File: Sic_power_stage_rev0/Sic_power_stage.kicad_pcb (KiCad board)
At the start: 4 copper layers, 265.1 x 88 mm, 176 parts, among them J1 20021321-00006C4LF, J2 20021321-00006C4LF, J3 20021321-00006C4LF, J4 20021321-00006C4LF, J5 20021321-00006C4LF, J6 20021321-00006C4LF, J7 20021321-00006C4LF, J8 20021321-00006C4LF, Q1 NTBG014N120M3P, Q10 NTBG014N120M3P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

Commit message: Define custom rules
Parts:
- moved STANDOFF19 161.1 mm to (36.5, 34.5)
- moved J1 143.1 mm to (52.5, -14.5)
- moved R12 137.7 mm to (-68.8, 16.9), turned to 180 degrees
- moved STANDOFF11 127.8 mm to (-113.5, -25.8)
- moved STANDOFF13 127.0 mm to (-69.0, 33.0)
- moved STANDOFF14 127.0 mm to (-58.0, 33.0)
- moved HOLE1 125.6 mm to (-270.1, -32.1)
- moved STANDOFF12 91.0 mm to (-80.0, 33.0)
- moved STANDOFF8 83.3 mm to (-113.0, -43.5)
- moved J3 69.0 mm to (-85.5, 23.5)
- moved J4 69.0 mm to (-52.5, 23.5)
- moved R13 40.6 mm to (-76.5, 16.9)
- moved J2 33.7 mm to (-21.5, 10.4)
- moved STANDOFF18 32.3 mm to (-145.0, -47.8)
- moved R6 27.6 mm to (-100.8, 10.2)
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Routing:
- net /Half Bridge A/G_TOP: track 30.7 -> 8.71 mm
- net /Half Bridge B/G_TOP: track 20.6 -> 4.58 mm, vias 0 -> 1
- net /Half Bridge A/S_BOT: track 0.00 -> 15.4 mm, vias 1 -> 0
- net /Half Bridge B/node_a: track 0.00 -> 12.1 mm
- net /Half Bridge B/D_BOT: track 23.8 -> 11.7 mm
- net /Half Bridge B/S_TOP: track 15.7 -> 6.30 mm, vias 0 -> 1
- net /Half Bridge A/D_TOP: track 22.5 -> 15.6 mm, vias 3 -> 2
- net /VBUS_M: track 6.50 -> 0.00 mm
- net /Half Bridge A/G_BOT: track 14.5 -> 20.6 mm, vias 1 -> 0
- net /Half Bridge B/S_BOT: track 6.05 -> 0.00 mm, vias 1 -> 0
- net /Half Bridge A/S_TOP: track 8.07 -> 2.95 mm
- net /Half Bridge B/G_BOT: track 4.58 -> 0.00 mm, vias 1 -> 0
- net PWRGND: track 17.6 -> 14.5 mm
- net /Half Bridge A/NTC_BOT: track 4.48 -> 2.48 mm
- net VBUS: vias 1464 -> 1466

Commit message: Redefine SiC layout
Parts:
- removed Q14, Q15, Q16: NTBG014N120M3P, Package_TO_SOT_SMD:TO-263-7_TabPin8
- removed Q19: IPN70R1K5CEATMA1, smd-semi:SOT-223-3
- removed R52, R53, R54, R55, R56, R57, R58, R59, R60, R61, R62, R63, R64, R65, R66, R67, R68, R69: R-1206, IPC7351-Nominal:RESC3216X60
- removed R70: R-0603, IPC7351-Nominal:RESC1608X50
- moved R20 244.3 mm to (-1.75, 62.2)
- moved R17 230.0 mm to (-4.25, 62.2), turned to -90 degrees
- moved R19 221.5 mm to (0.65, 62.2)
- moved STANDOFF18 218.5 mm to (58.0, 33.0)
- moved R16 208.9 mm to (-6.75, 62.2), turned to -90 degrees
- moved STANDOFF15 197.7 mm to (-106.0, 100.0)
- moved STANDOFF20 193.0 mm to (80.0, 33.0)
- moved HOLE5 178.9 mm to (-141.2, -19.5)
- moved C33 178.7 mm to (99.5, -19.5), turned to 180 degrees
- moved C27 174.4 mm to (-176.2, 37.8)
- moved C28 174.4 mm to (-126.4, 32.9)
- moved C40 174.4 mm to (-159.6, 47.7)
- moved R46 174.4 mm to (-142.4, 24.4)
- moved R47 174.4 mm to (-142.4, 27.7)
- moved R48 174.4 mm to (-142.4, 31.1)
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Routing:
- net /Half Bridge C/S_TOP: track 156.8 -> 0.00 mm, vias 3 -> 0
- net /Half Bridge C/S_BOT: track 129.5 -> 0.00 mm, vias 3 -> 0
- net /Half Bridge C/G_BOT: track 122.0 -> 0.00 mm, vias 2 -> 0
- net /Half Bridge C/G_TOP: track 110.7 -> 0.00 mm, vias 3 -> 0
- net /Half Bridge C/SHUNT-: track 23.5 -> 0.00 mm
- net /Half Bridge B/SHUNT-: track 22.9 -> 0.00 mm
- net /Half Bridge C/SHUNT+: track 22.8 -> 0.00 mm
- net /Half Bridge B/SHUNT+: track 22.2 -> 0.00 mm
- net /Half Bridge A/G_BOT: track 20.6 -> 0.00 mm
- net /Half Bridge A/D_TOP: track 15.6 -> 0.00 mm, vias 2 -> 0
- net /Half Bridge A/S_BOT: track 15.4 -> 0.00 mm
- net /Half Bridge B/D_TOP: track 15.1 -> 0.35 mm, vias 0 -> 1
- net (no net): track 16.7 -> 2.66 mm
- net /Half Bridge B/node_a: track 12.1 -> 0.00 mm
- net /Half Bridge B/D_BOT: track 11.7 -> 0.00 mm
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- added copper zone on F.Cu, net /Half Bridge B/node_a
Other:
- board size 265.1 x 88 mm -> 241.3 x 91 mm

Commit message: Add minor changes
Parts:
- moved D4 88.8 mm to (-62.2, 19.5)
- moved R18 72.9 mm to (20.5, 3.00)
- moved R20 72.3 mm to (19.8, -6.75), turned to 180 degrees
- moved D10 71.6 mm to (42.8, 25.2)
- moved R19 70.5 mm to (-14.0, -6.75), turned to 180 degrees
- moved D7 69.8 mm to (-23.8, 30.5), turned to -90 degrees
- moved R17 59.9 mm to (-12.8, 3.00), turned to 0 degrees
- moved D3 58.8 mm to (-105.8, 9.50), turned to -90 degrees
- moved R6 45.5 mm to (-59.8, 17.5)
- moved D2 35.1 mm to (-57.8, 20.8)
- moved C2 34.7 mm to (-55.2, 18.8)
- moved C10 27.5 mm to (-79.5, -22.0), turned to 90 degrees
- moved C11 27.5 mm to (-60.5, -49.5), turned to -90 degrees
- moved C12 27.5 mm to (-41.5, -22.0), turned to 90 degrees
- moved C22 27.5 mm to (-24.2, -49.5), turned to -90 degrees
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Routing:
- net (no net): track 2.66 -> 0.16 mm
- net PWRGND: track 10.4 -> 8.87 mm
- net Net-(DS1-A): track 1.73 -> 1.00 mm
- net VBUS: track 0.00 -> 0.01 mm, vias 4 -> 1
- removed copper zone on B.Cu, net PWRGND
- removed copper zone on B.Cu, net VBUS

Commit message: Re allocate film capacitors and re define layout for power mosfet
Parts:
- moved C38 10.2 mm to (99.0, -25.0)
- moved C12 9.77 mm to (-50.8, -25.0)
- moved C25 9.01 mm to (24.2, -25.0)
- moved C9 8.50 mm to (-90.5, -52.5)
- moved C22 8.31 mm to (-16.5, -52.5)
- moved C35 6.35 mm to (57.2, -52.8)
- moved C33 4.76 mm to (94.8, -19.2)
- moved C34 4.76 mm to (94.8, -13.2)
- moved C37 4.28 mm to (86.8, -52.5)
- moved C11 3.50 mm to (-62.2, -52.5)
- moved C24 3.35 mm to (12.2, -52.5)
- moved C36 3.35 mm to (70.0, -25.2)
- moved C20 3.20 mm to (20.2, -19.2)
- moved C21 3.20 mm to (20.2, -13.2)
- moved C23 3.09 mm to (-4.50, -25.0)
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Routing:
- added copper zone on B.Cu, net PWRGND
- added copper zone on In1.Cu, net PWRGND
- added copper zone on B.Cu, net VBUS
- added copper zone on In1.Cu, net VBUS

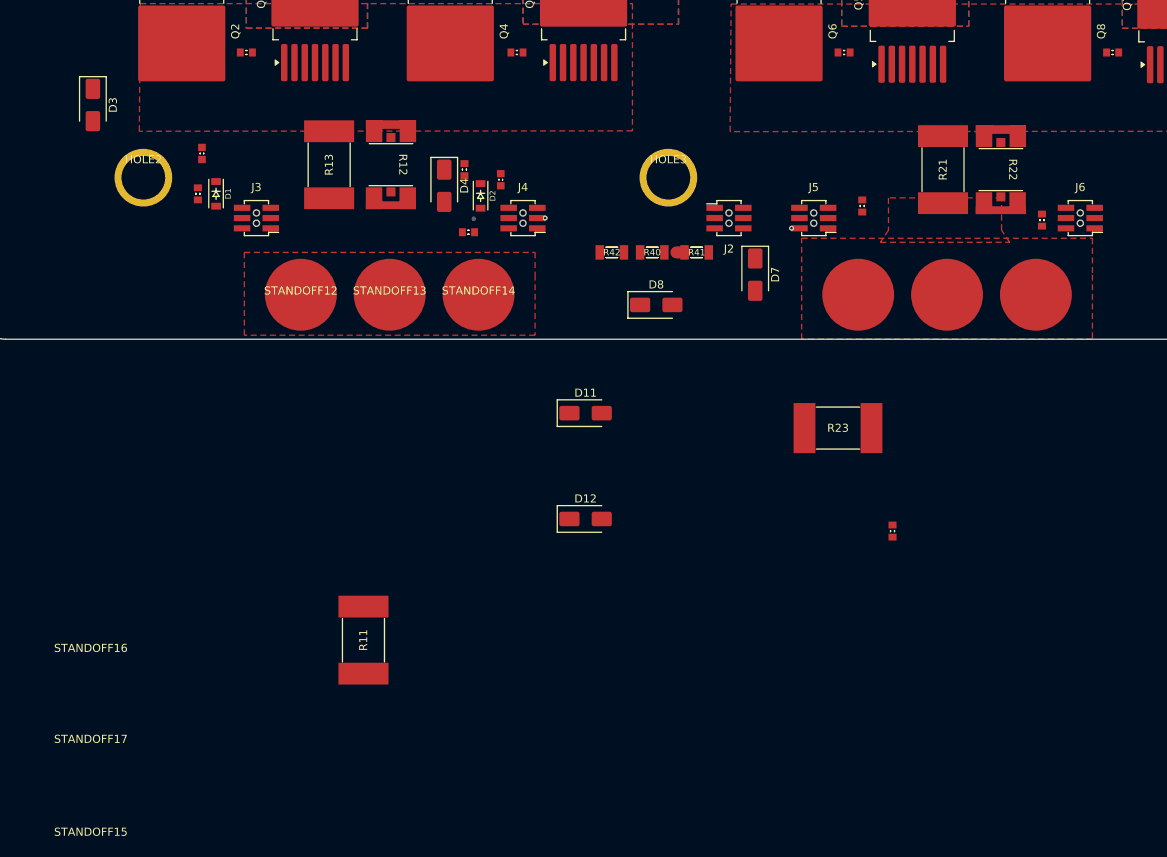
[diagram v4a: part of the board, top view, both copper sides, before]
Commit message: Add traces for leg A referring to gate and driver source
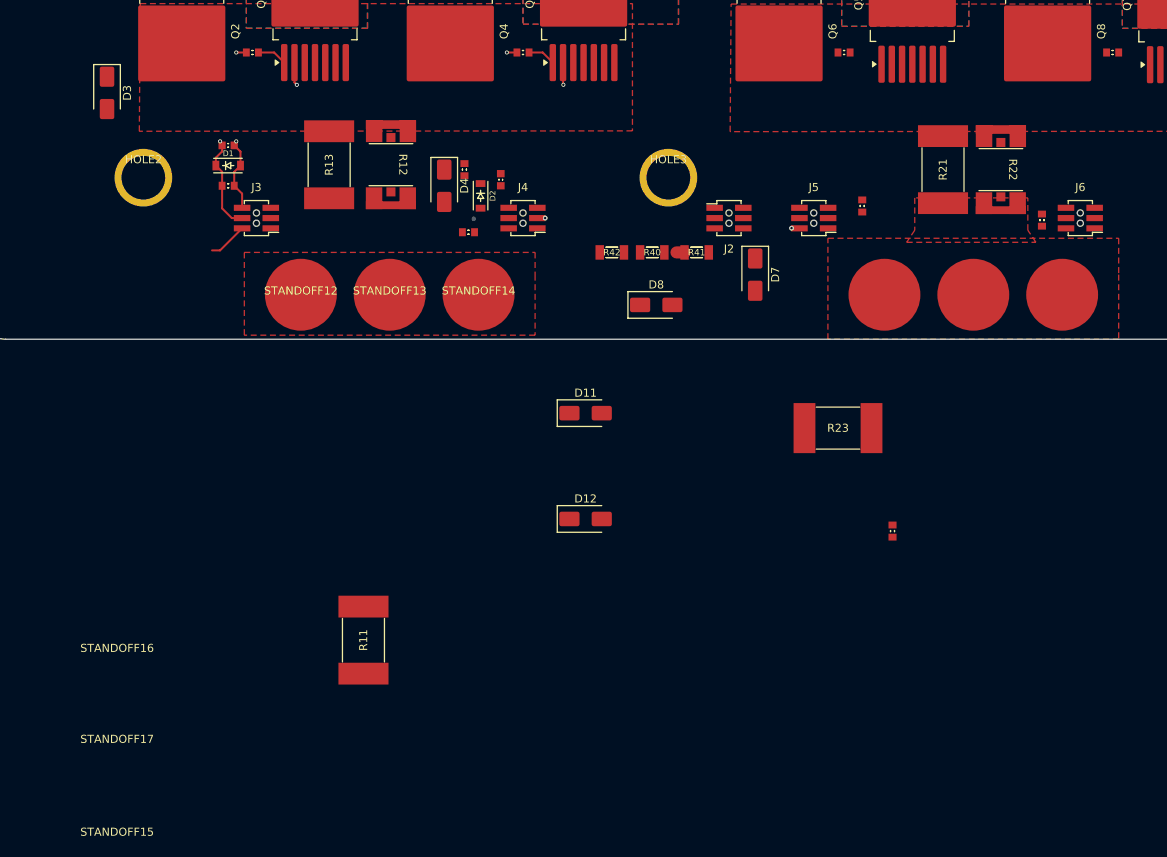
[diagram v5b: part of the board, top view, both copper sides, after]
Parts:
- moved R5 3.88 mm to (-89.0, 19.5), turned to 0 degrees
- moved D1 3.81 mm to (-89.0, 17.0), turned to 0 degrees
- moved C1 3.40 mm to (-89.0, 14.5), turned to 0 degrees
- moved STANDOFF15 3.25 mm to (-102.8, 100.0)
- moved STANDOFF16 3.25 mm to (-102.8, 77.2)
- moved STANDOFF17 3.25 mm to (-102.8, 88.5)
- moved D3 2.30 mm to (-104.0, 8.00)
- moved R7 0.75 mm to (-86.0, 3.00)
- moved R8 0.75 mm to (-52.5, 3.00)
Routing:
- net /Half Bridge A/S_TOP: track 0.03 -> 102.9 mm, vias 0 -> 3
- net /Half Bridge A/G_TOP: track 0.00 -> 75.7 mm, vias 0 -> 3
- net /Half Bridge A/D_TOP: track 0.00 -> 4.86 mm
- net /Half Bridge A/GT1: track 0.00 -> 3.71 mm
- net /Half Bridge A/GT2: track 0.00 -> 3.46 mm

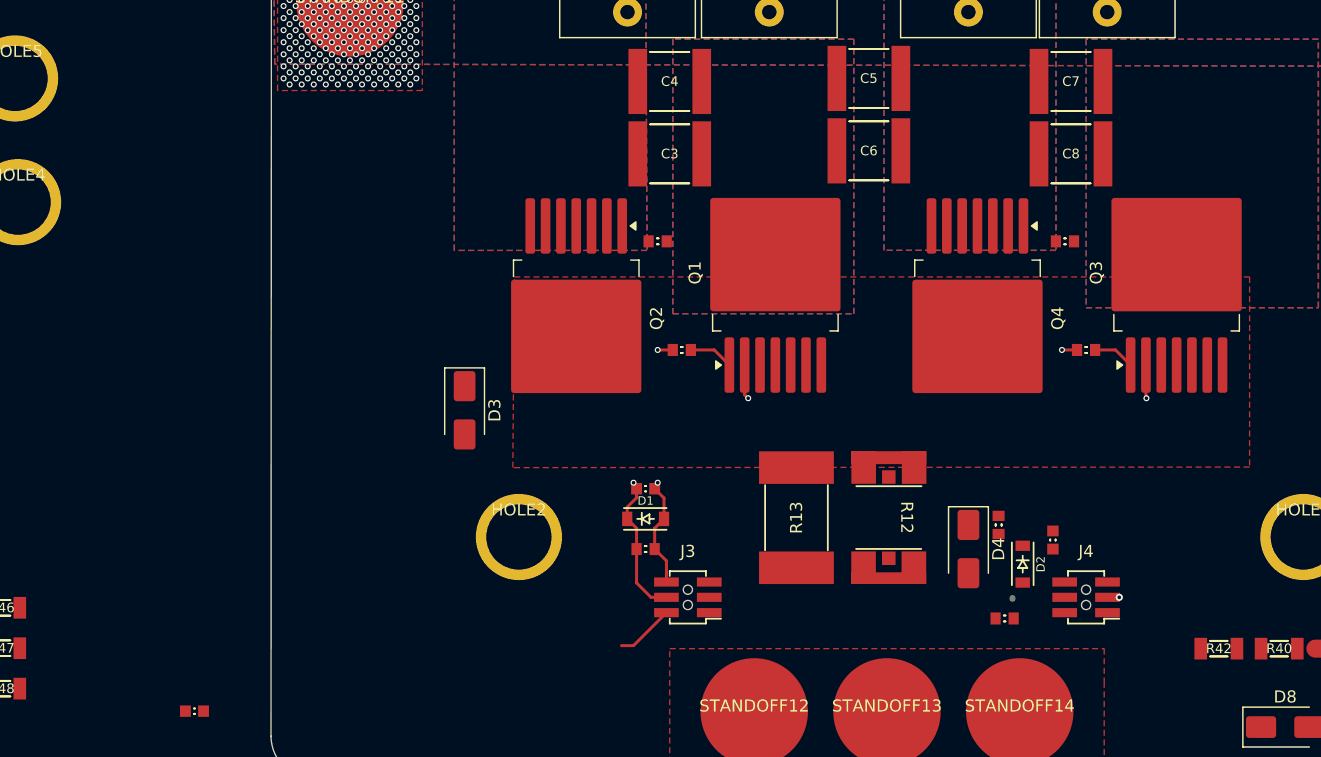
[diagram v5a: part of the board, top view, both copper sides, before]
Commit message: Add tentative routing for leg A
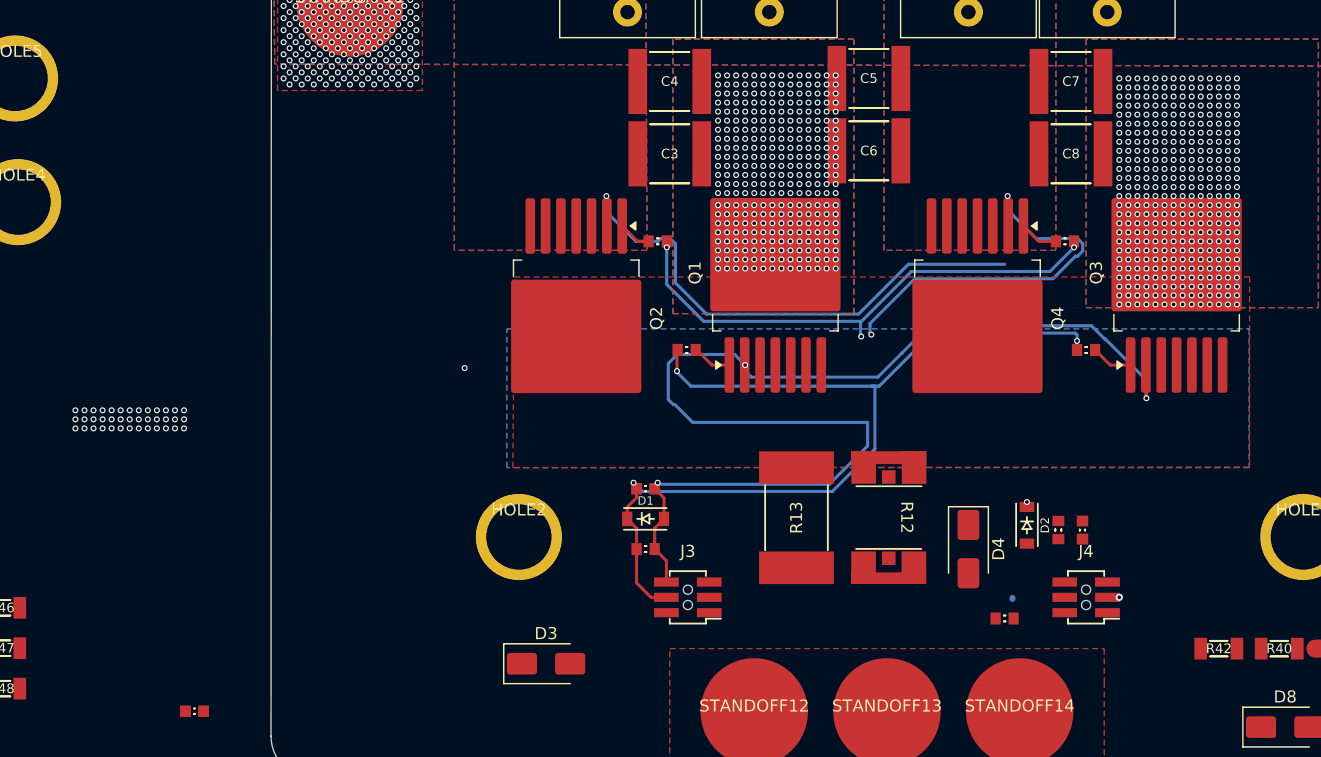
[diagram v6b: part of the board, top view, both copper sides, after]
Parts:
- moved D3 22.1 mm to (-97.2, 29.0), turned to 0 degrees
- moved R6 4.97 mm to (-54.8, 17.9), turned to -90 degrees
- moved D2 3.24 mm to (-57.4, 17.5)
- moved C2 2.59 mm to (-52.8, 17.9), turned to -90 degrees
- moved R7 0.40 mm to (-85.6, 3.00)
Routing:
- net /Half Bridge A/S_BOT: track 0.00 -> 101.0 mm, vias 0 -> 3
- net /Half Bridge A/G_BOT: track 0.00 -> 67.7 mm, vias 0 -> 4
- net /Half Bridge A/D_TOP: track 4.86 -> 0.00 mm
- net /Half Bridge A/S_TOP: track 102.9 -> 99.3 mm
- net /Half Bridge A/G_bottom_2: track 0.00 -> 3.22 mm
- net /Half Bridge A/G_bottom_1: track 0.00 -> 2.72 mm
- net /Half Bridge A/G_TOP: track 75.7 -> 77.9 mm
- net VBUS: vias 1 -> 674
- net /Half Bridge A/node_a: vias 0 -> 39
- added copper zone on B.Cu, net /Half Bridge A/node_a

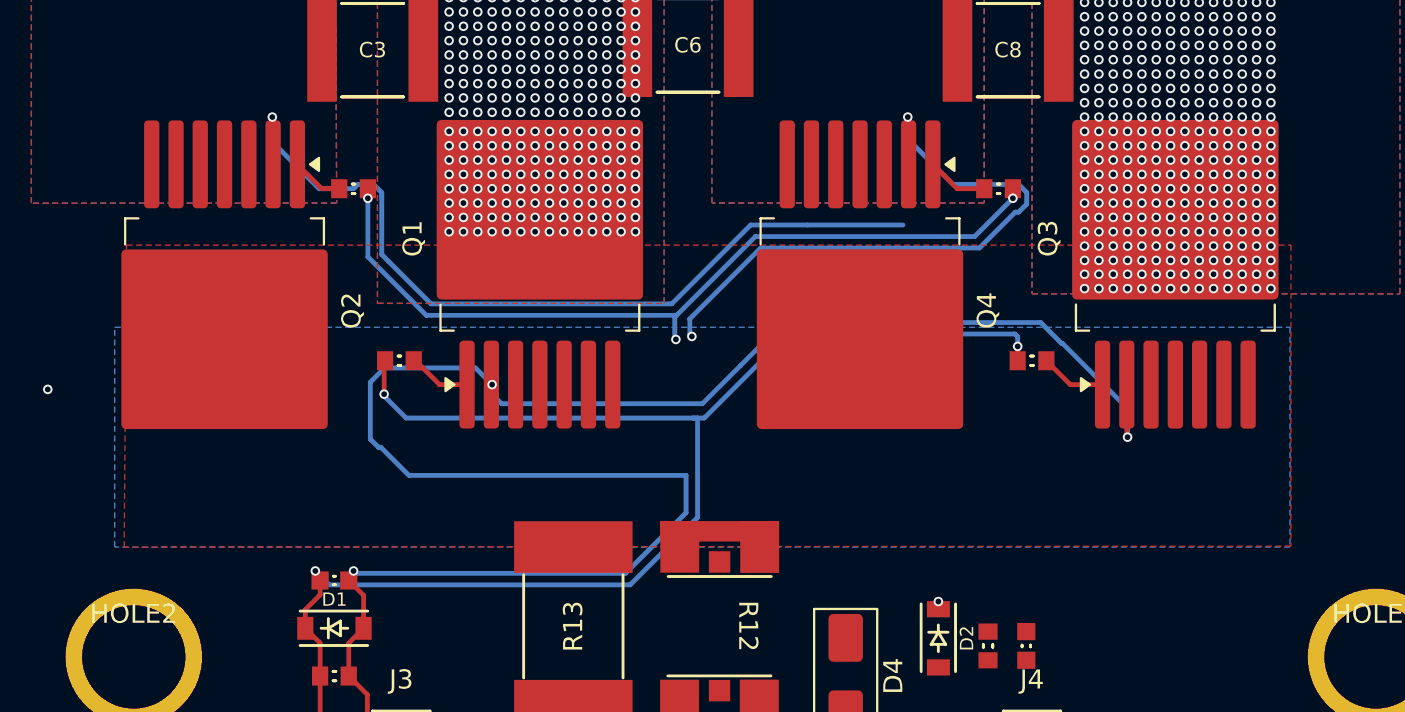
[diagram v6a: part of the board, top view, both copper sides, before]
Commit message: Add traces for LEG-A, tentative place for main power supply
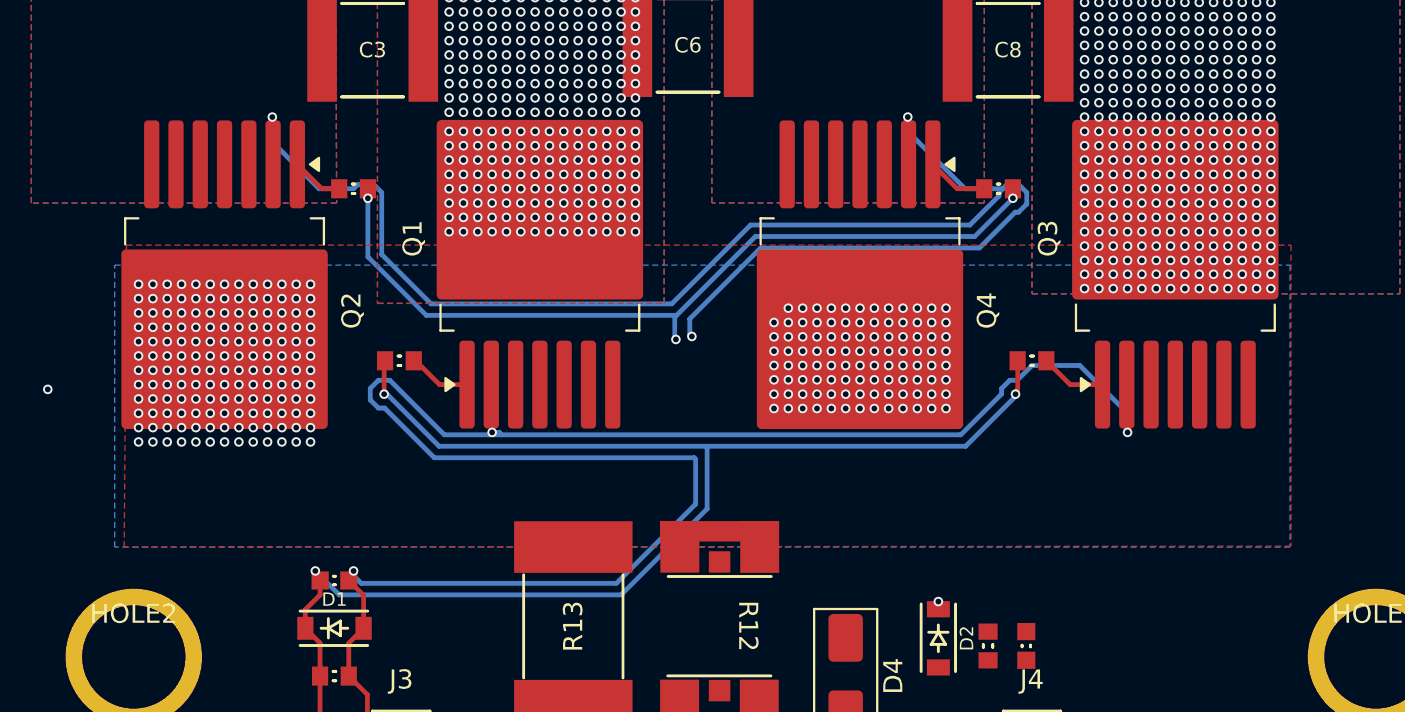
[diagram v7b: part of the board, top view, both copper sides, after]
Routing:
- net /Half Bridge A/S_BOT: track 101.0 -> 105.3 mm
- net /Half Bridge A/S_TOP: track 99.3 -> 100.9 mm
- net /Half Bridge A/G_BOT: track 67.7 -> 66.4 mm
- net /Half Bridge A/G_TOP: track 77.9 -> 77.1 mm
- net /Half Bridge A/node_a: vias 39 -> 298
- added copper zone on In2.Cu, net /Half Bridge A/node_a

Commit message: SiC: routing phase A and B - place components
Signed-off-by: Ayarde Christian <cayarde@paltatech.com>
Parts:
- moved STANDOFF11 154.4 mm to (39.8, -44.5)
- moved C40 139.2 mm to (-22.5, 23.5)
- moved R1 131.0 mm to (-34.5, 9.75), turned to 0 degrees
- moved D12 111.5 mm to (58.2, 18.0)
- moved C15 99.9 mm to (14.4, 15.3), turned to 0 degrees
- moved R35 94.5 mm to (-36.0, 5.50)
- moved C14 86.9 mm to (-16.5, 15.0), turned to 180 degrees
- moved R34 85.1 mm to (-33.2, 5.50), turned to 90 degrees
- moved R36 81.4 mm to (-34.8, 0.50), turned to 90 degrees
- moved D11 81.3 mm to (34.5, 29.5)
- moved STANDOFF8 79.8 mm to (-33.2, -45.0)
- moved D6 77.7 mm to (14.7, 19.6), turned to 0 degrees
- moved D5 71.0 mm to (-16.5, 19.5), turned to 180 degrees
- moved R16 49.7 mm to (14.4, 17.3), turned to 0 degrees
- moved R40 42.5 mm to (-68.2, 56.0)
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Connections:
- R34 pad 1: Net-(R34-Pad1) -> /VBUS_M
- R35 pad 1: /VBUS_M -> Net-(R34-Pad2)
- R35 pad 2: Net-(R34-Pad1) -> Net-(R35-Pad2)
- R36 pad 1: Net-(R34-Pad2) -> Net-(R35-Pad2)
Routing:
- net /Half Bridge B/S_TOP: track 1.82 -> 92.5 mm, vias 0 -> 3
- net /Half Bridge B/S_BOT: track 0.00 -> 84.3 mm, vias 0 -> 4
- net /Half Bridge B/G_TOP: track 0.00 -> 64.1 mm, vias 0 -> 3
- net VBUS: track 0.01 -> 62.9 mm, vias 674 -> 1345
- net /Half Bridge B/G_BOT: track 0.00 -> 62.3 mm, vias 0 -> 4
- net /Half Bridge A/NTC_BOT: track 0.00 -> 41.1 mm, vias 0 -> 2
- net /Half Bridge A/SHUNT-: track 0.00 -> 24.5 mm
- net /Half Bridge A/SHUNT+: track 0.00 -> 24.2 mm
- net /Half Bridge A/S_BOT: track 105.3 -> 87.1 mm
- net /VBUS_M: track 0.00 -> 5.79 mm
- net /Half Bridge B/GT1: track 0.00 -> 5.33 mm
- net /Half Bridge B/GT2: track 0.00 -> 4.27 mm
- net Net-(R34-Pad2): track 0.00 -> 4.14 mm
- net /Half Bridge A/node_a: track 0.00 -> 3.75 mm
- net /Half Bridge B/G_bottom_2: track 0.00 -> 2.96 mm
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- added copper zone on B.Cu, net /Half Bridge B/node_a
- added copper zone on In2.Cu, net /Half Bridge B/node_a
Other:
- board size 241.3 x 91 mm -> 242.5 x 94.5 mm
- board text added: "Clearance reduced to match with a lower voltage"
